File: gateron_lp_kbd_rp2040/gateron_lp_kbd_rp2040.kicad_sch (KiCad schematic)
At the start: 238 parts, among them J1 TYPE-C-31-M-12, J2 JST-SH-2 SM02B, Q1 DMG3415U, SW1 KS-33, SW10 KS-33, SW11 KS-33, SW12 KS-33, SW13 KS-33, SW14 KS-33, SW15 KS-33, SW16 KS-33, SW17 KS-33, SW18 KS-33, SW19 KS-33, SW2 KS-33, SW20 KS-33, SW21 KS-33, SW22 KS-33, SW23 KS-33, SW24 KS-33, SW25 KS-33, SW26 KS-33, SW27 KS-33, SW28 KS-33, SW29 KS-33, SW3 KS-33, SW30 KS-33, SW31 KS-33, SW32 KS-33, SW33 KS-33, SW34 KS-33, SW35 KS-33, SW36 KS-33, SW37 KS-33, SW38 KS-33, SW39 KS-33, SW4 KS-33, SW40 KS-33, SW41 KS-33, SW42 KS-33, SW43 KS-33, SW44 KS-33, SW45 KS-33, SW46 KS-33, SW47 KS-33, SW48 KS-33, SW49 KS-33, SW5 KS-33, SW50 KS-33, SW51 KS-33, SW52 KS-33, SW53 KS-33, SW54 2U, SW55 KS-33, SW56 KS-33, SW57 KS-33, SW58 KS-33, SW59 KS-33, SW6 KS-33, SW60 RESET, SW61 BOOTSEL (VERIFY), SW62 PWR MSK-12C02, SW7 KS-33, SW8 KS-33, SW9 KS-33, U1 RP2040, U2 MCP73831-2ACI/OT, U3 AP2112K-3.3, U4 USBLC6-2SC6, U5 W25Q16JVUXIQ, U6 CYW43439, U7 74AHCT1G125, Y1 12MHz, Y2 37.4MHz

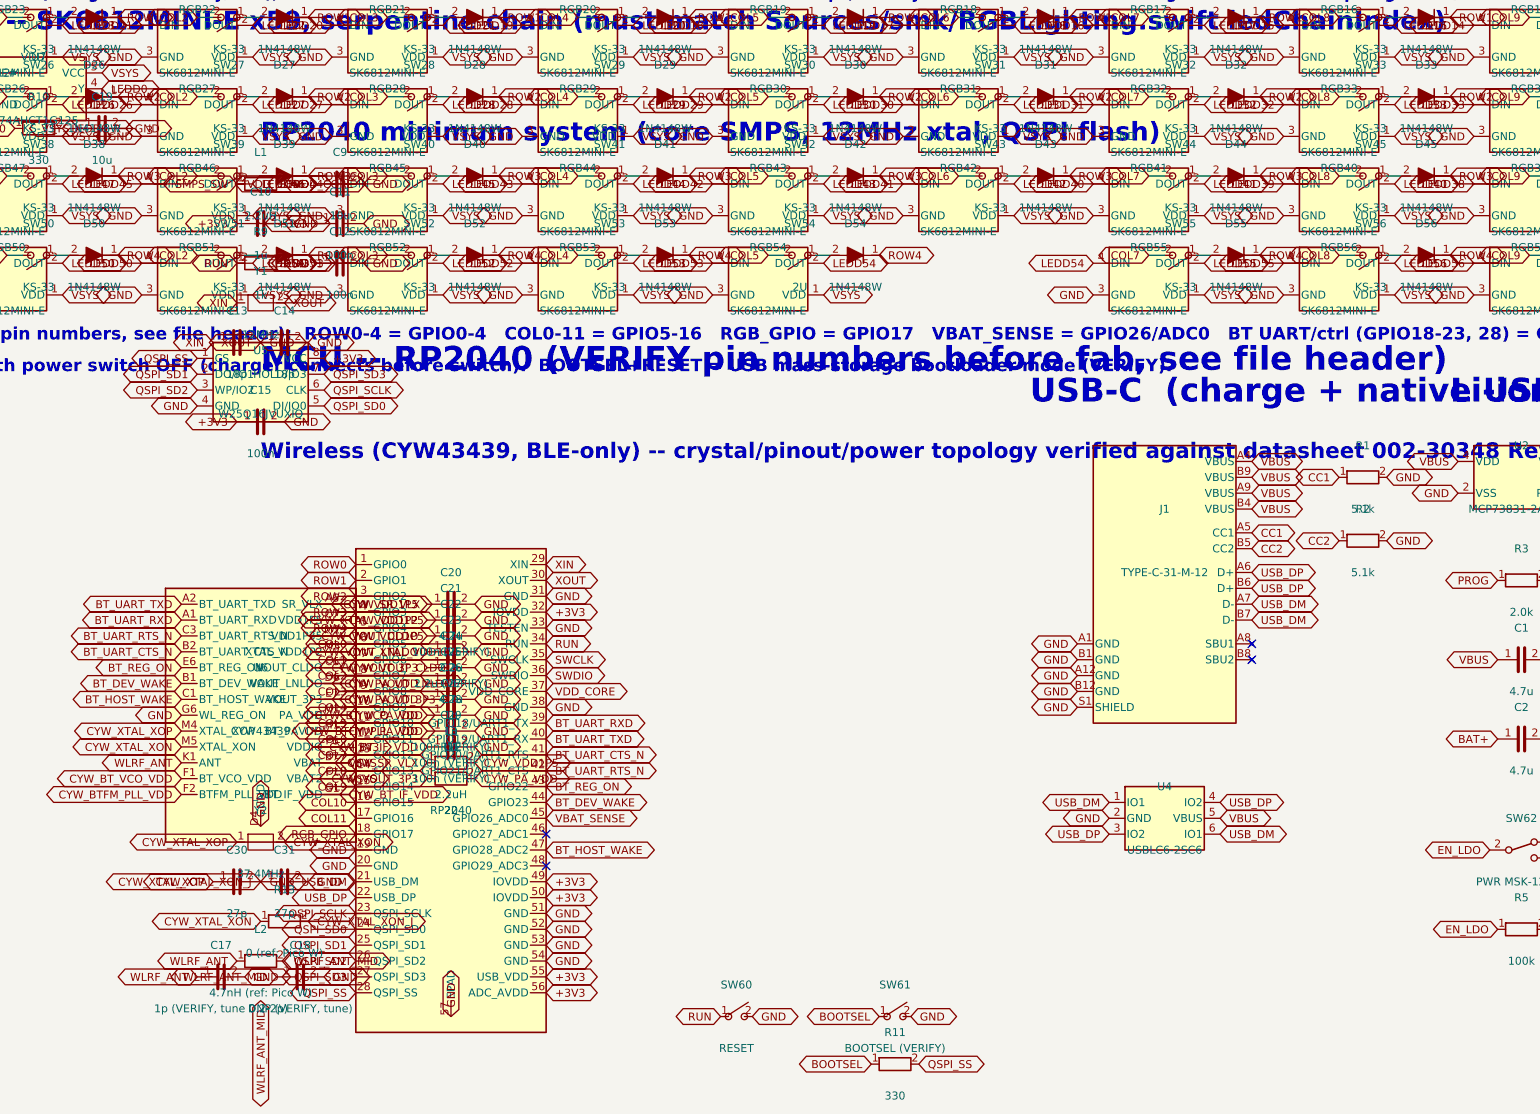
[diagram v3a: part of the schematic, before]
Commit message: Verify RP2040 pin numbers against the real datasheet, fix two real bugs
Pin numbers, dedicated-pin names, and QFN-56 side rotation now come from
Raspberry Pi's own RP2040 datasheet (Fig. 3, Table 1, Table 2) instead of
an invented sequential scheme. This caught two real design bugs:

- The core supply was modeled as a buck regulator needing an external
  inductor (L1, 2.2uH). The real on-chip regulator (Section 2.10, "Core
  Supply Regulator") is a linear/LDO type -- VREG_VIN -> VREG_VOUT -> DVDD
  -- needing only decoupling capacitors. L1 is removed; C9/C32/C33/C34 now
  match the datasheet's own application circuit (Figure 20).
- The BT UART was wired to GPIO18-21, but UART1's real alternate-function
  pins are GPIO20-23 (Table 2) -- GPIO18/19 (no alt-function needed) now
  carry BT_REG_ON/BT_DEV_WAKE instead, freeing GPIO20-23 for the actual
  UART1 TX/RX/CTS/RTS.

Also fixed: the real chip has no perimeter GND pins (GND is only the
single exposed thermal pad) -- removed several invented ones. And caught,
independently of the pinout work, two schematic label collisions (C13/C14
and C30/C31 crystal load caps landing global labels of different nets on
the identical coordinate, which can short a net to GND in the extracted
netlist) -- widened spacing to fix both.

Verified via kicad-happy analyzers: zero new errors/warnings, zero
courtyard or keepout collisions, zero schematic label collisions anywhere
in the file (full-file scan, not just the touched areas).

Co-Authored-By: Claude Sonnet 5 <noreply@anthropic.com>
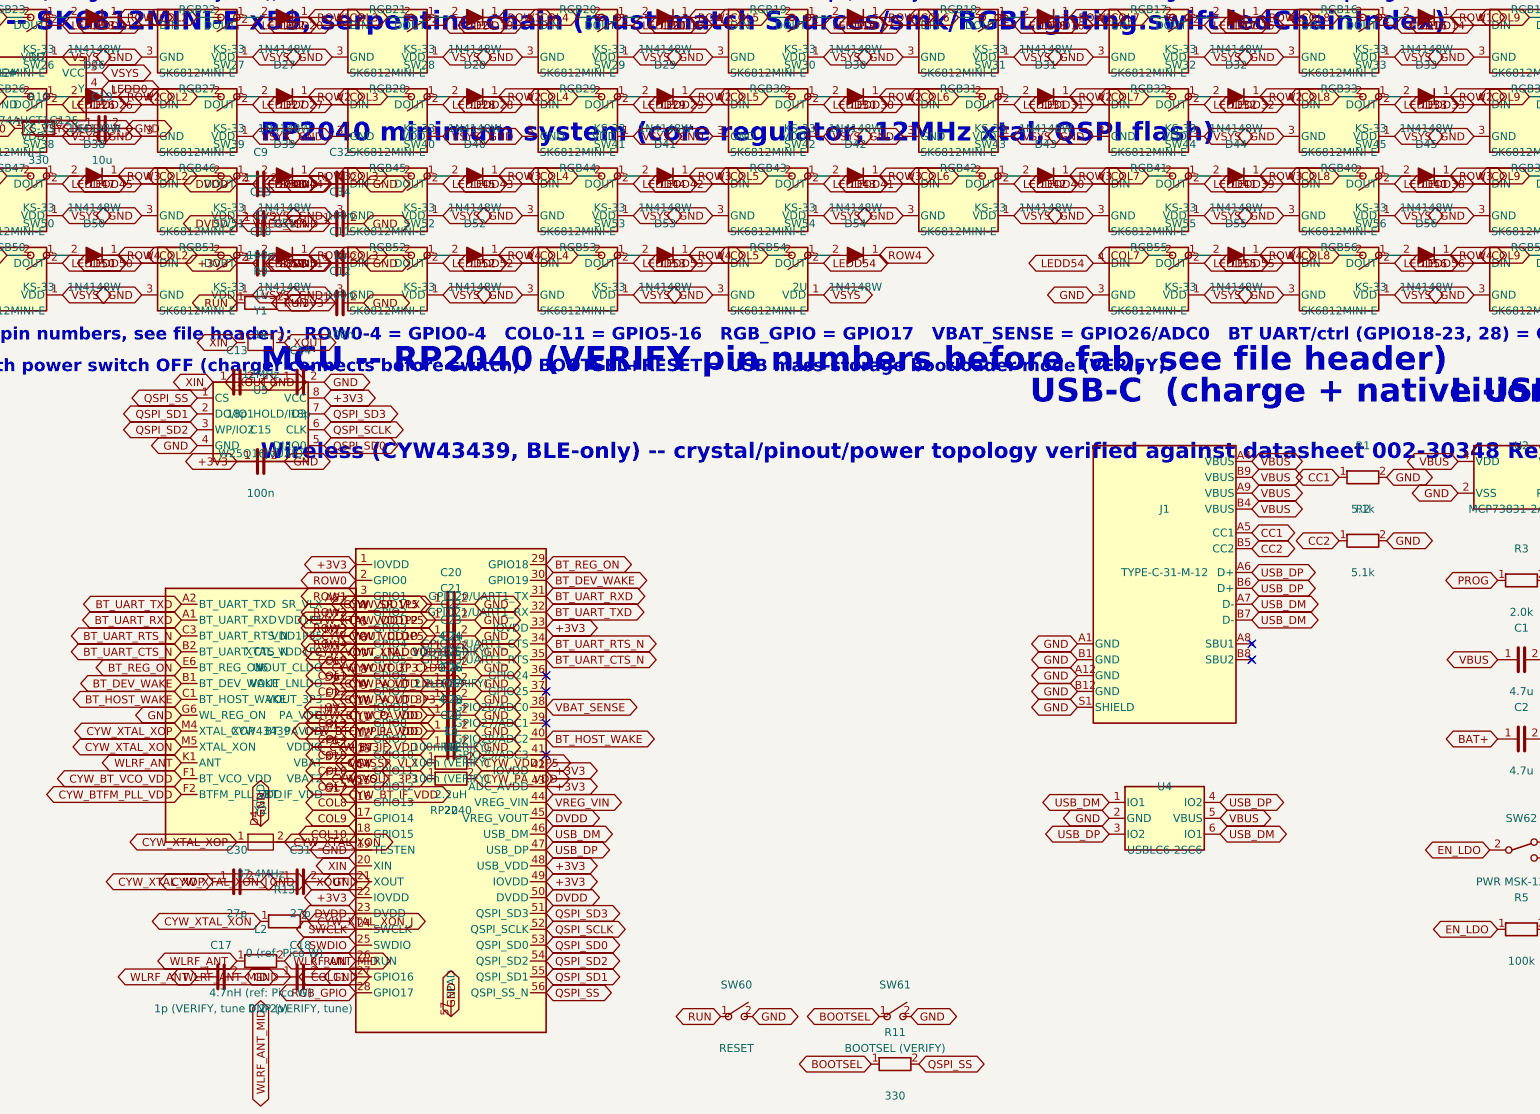
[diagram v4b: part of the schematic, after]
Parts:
- removed L1: 2.2uH, kbd:RC_0603, symbol kbd:R_kbd
- added C32, C33: 100n, kbd:RC_0603, symbol kbd:C_kbd
- added C34: 1u, kbd:RC_0603, symbol kbd:C_kbd
- C9: value 10u -> 1u
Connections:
- net +3V3: now also U1.1 (IOVDD), U1.10 (IOVDD), U1.22 (IOVDD), U1.33 (IOVDD), U1.42 (IOVDD), U1.43 (ADC_AVDD), U1.48 (USB_VDD); no longer U1.32 (IOVDD), U1.50 (IOVDD), U1.55 (USB_VDD), U1.56 (ADC_AVDD)
- net BT_DEV_WAKE: now also U1.30 (GPIO19); no longer U1.44 (GPIO23)
- net BT_HOST_WAKE: now also U1.40 (GPIO28/ADC2); no longer U1.47 (GPIO28_ADC2)
- net BT_REG_ON: now also U1.29 (GPIO18); no longer U1.43 (GPIO22)
- net BT_UART_CTS_N: now also U1.35 (GPIO23/UART1_RTS); no longer U1.41 (GPIO20/UART1_RTS)
- net BT_UART_RTS_N: now also U1.34 (GPIO22/UART1_CTS); no longer U1.42 (GPIO21/UART1_CTS)
- net BT_UART_RXD: now also U1.31 (GPIO20/UART1_TX); no longer U1.39 (GPIO18/UART1_TX)
- net BT_UART_TXD: now also U1.32 (GPIO21/UART1_RX); no longer U1.40 (GPIO19/UART1_RX)
- net COL0: now also U1.7 (GPIO5); no longer U1.6 (GPIO5)
- net COL1: now also U1.8 (GPIO6); no longer U1.7 (GPIO6)
- net COL10: now also U1.18 (GPIO15); no longer U1.16 (GPIO15)
- net COL11: now also U1.27 (GPIO16); no longer U1.17 (GPIO16)
- net COL2: now also U1.9 (GPIO7); no longer U1.8 (GPIO7)
- net COL3: now also U1.11 (GPIO8); no longer U1.9 (GPIO8)
- net COL4: now also U1.12 (GPIO9); no longer U1.10 (GPIO9)
- net COL5: now also U1.13 (GPIO10); no longer U1.11 (GPIO10)
- net COL6: now also U1.14 (GPIO11); no longer U1.12 (GPIO11)
- net COL7: now also U1.15 (GPIO12); no longer U1.13 (GPIO12)
- net COL8: now also U1.16 (GPIO13); no longer U1.14 (GPIO13)
- net COL9: now also U1.17 (GPIO14); no longer U1.15 (GPIO14)
- net CYW_XTAL_XON_J: no longer C1.2, C10.2, C11.2, C12.2, C13.2, C14.1, C14.2, C15.2, C17.2, C18.2, C19.2, C2.2, C20.2, C21.2, C22.2, C23.2, C24.2, C25.2, C26.2, C27.2, C28.2, C29.2, C3.2, C30.2, C31.2, C4.2, C5.2, C7.2, C8.2, C9.2, J1.A1 (GND), J1.A12 (GND), J1.B1 (GND), J1.B12 (GND), J1.S1 (SHIELD), J2.2 (BAT-), R1.2, R2.2, R3.2, R5.2, R7.2, RGB1.3 (GND), RGB10.3 (GND), RGB11.3 (GND), RGB12.3 (GND), RGB13.3 (GND), RGB14.3 (GND), RGB15.3 (GND), RGB16.3 (GND), RGB17.3 (GND), RGB18.3 (GND), RGB19.3 (GND), RGB2.3 (GND), RGB20.3 (GND), RGB21.3 (GND), RGB22.3 (GND), RGB23.3 (GND), RGB24.3 (GND), RGB25.3 (GND), RGB26.3 (GND), RGB27.3 (GND), RGB28.3 (GND), RGB29.3 (GND), RGB3.3 (GND), RGB30.3 (GND), RGB31.3 (GND), RGB32.3 (GND), RGB33.3 (GND), RGB34.3 (GND), RGB35.3 (GND), RGB36.3 (GND), RGB37.3 (GND), RGB38.3 (GND), RGB39.3 (GND), RGB4.3 (GND), RGB40.3 (GND), RGB41.3 (GND), RGB42.3 (GND), RGB43.3 (GND), RGB44.3 (GND), RGB45.3 (GND), RGB46.3 (GND), RGB47.3 (GND), RGB48.3 (GND), RGB49.3 (GND), RGB5.3 (GND), RGB50.3 (GND), RGB51.3 (GND), RGB52.3 (GND), RGB53.3 (GND), RGB54.3 (GND), RGB55.3 (GND), RGB56.3 (GND), RGB57.3 (GND), RGB58.3 (GND), RGB59.3 (GND), RGB6.3 (GND), RGB7.3 (GND), RGB8.3 (GND), RGB9.3 (GND), SW60.2, SW61.2, SW62.3 (B), U1.19 (GND), U1.20 (GND), U1.30 (XOUT), U1.31 (GND), U1.33 (TESTEN), U1.38 (GND), U1.51 (GND), U1.52 (GND), U1.53 (GND), U1.54 (GND), U1.57 (EPAD), U2.2 (VSS), U3.2 (GND), U4.2 (GND), U5.4 (GND), U6.D4 (GND), U6.G6 (WL_REG_ON), U7.1 (OE#), U7.3 (GND), Y1.2
- net QSPI_SCLK: now also U1.52 (QSPI_SCLK); no longer U1.23 (QSPI_SCLK)
- net QSPI_SD0: now also U1.53 (QSPI_SD0); no longer U1.24 (QSPI_SD0)
- net QSPI_SD1: now also U1.55 (QSPI_SD1); no longer U1.25 (QSPI_SD1)
- net QSPI_SD2: now also U1.54 (QSPI_SD2); no longer U1.26 (QSPI_SD2)
- net QSPI_SD3: now also U1.51 (QSPI_SD3); no longer U1.27 (QSPI_SD3)
- net QSPI_SS: now also U1.56 (QSPI_SS_N); no longer U1.28 (QSPI_SS)
- net RGB_GPIO: now also U1.28 (GPIO17); no longer U1.18 (GPIO17)
- net ROW0: now also U1.2 (GPIO0); no longer U1.1 (GPIO0)
- net ROW1: now also U1.3 (GPIO1); no longer U1.2 (GPIO1)
- net ROW2: now also U1.4 (GPIO2); no longer U1.3 (GPIO2)
- net ROW3: now also U1.5 (GPIO3); no longer U1.4 (GPIO3)
- net ROW4: now also U1.6 (GPIO4); no longer U1.5 (GPIO4)
- net RUN: now also U1.26 (RUN); no longer U1.34 (RUN)
- net SWCLK: now also U1.24 (SWCLK); no longer U1.35 (SWCLK)
- net SWDIO: now also U1.25 (SWDIO); no longer U1.36 (SWDIO)
- net USB_DM: now also U1.46 (USB_DM); no longer U1.21 (USB_DM)
- net USB_DP: now also U1.47 (USB_DP); no longer U1.22 (USB_DP)
- net VBAT_SENSE: now also U1.38 (GPIO26/ADC0); no longer U1.45 (GPIO26_ADC0)
- net XIN: now also U1.20 (XIN); no longer U1.29 (XIN)
- net VDD_CORE: no longer names the net of U1.37 (GPIO25)
- net VDD_CORE: no longer C9.1
- new net DVDD: C32.1, C33.1, C9.1, U1.23 (DVDD), U1.45 (VREG_VOUT), U1.50 (DVDD)
- new net GND: C1.2, C10.2, C11.2, C12.2, C13.2, C14.2, C15.2, C17.2, C18.2, C19.2, C2.2, C20.2, C21.2, C22.2, C23.2, C24.2, C25.2, C26.2, C27.2, C28.2, C29.2, C3.2, C30.2, C31.2, C32.2, C33.2, C34.2, C4.2, C5.2, C7.2, C8.2, C9.2, J1.A1 (GND), J1.A12 (GND), J1.B1 (GND), J1.B12 (GND), J1.S1 (SHIELD), J2.2 (BAT-), R1.2, R2.2, R3.2, R5.2, R7.2, RGB1.3 (GND), RGB10.3 (GND), RGB11.3 (GND), RGB12.3 (GND), RGB13.3 (GND), RGB14.3 (GND), RGB15.3 (GND), RGB16.3 (GND), RGB17.3 (GND), RGB18.3 (GND), RGB19.3 (GND), RGB2.3 (GND), RGB20.3 (GND), RGB21.3 (GND), RGB22.3 (GND), RGB23.3 (GND), RGB24.3 (GND), RGB25.3 (GND), RGB26.3 (GND), RGB27.3 (GND), RGB28.3 (GND), RGB29.3 (GND), RGB3.3 (GND), RGB30.3 (GND), RGB31.3 (GND), RGB32.3 (GND), RGB33.3 (GND), RGB34.3 (GND), RGB35.3 (GND), RGB36.3 (GND), RGB37.3 (GND), RGB38.3 (GND), RGB39.3 (GND), RGB4.3 (GND), RGB40.3 (GND), RGB41.3 (GND), RGB42.3 (GND), RGB43.3 (GND), RGB44.3 (GND), RGB45.3 (GND), RGB46.3 (GND), RGB47.3 (GND), RGB48.3 (GND), RGB49.3 (GND), RGB5.3 (GND), RGB50.3 (GND), RGB51.3 (GND), RGB52.3 (GND), RGB53.3 (GND), RGB54.3 (GND), RGB55.3 (GND), RGB56.3 (GND), RGB57.3 (GND), RGB58.3 (GND), RGB59.3 (GND), RGB6.3 (GND), RGB7.3 (GND), RGB8.3 (GND), RGB9.3 (GND), SW60.2, SW61.2, SW62.3 (B), U1.19 (TESTEN), U1.57 (EPAD), U2.2 (VSS), U3.2 (GND), U4.2 (GND), U5.4 (GND), U6.D4 (GND), U6.G6 (WL_REG_ON), U7.1 (OE#), U7.3 (GND)
- new net VREG_VIN: C34.1, U1.44 (VREG_VIN)
- new net XOUT: C14.1, U1.21 (XOUT), Y1.2
- no-connect marks 6 -> 8
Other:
- note added: "RP2040 minimum system (core regulator, 12MHz xtal, QSPI flash)"
- note removed: "RP2040 minimum system (core SMPS, 12MHz xtal, QSPI flash)"
- moved on the sheet: C10, C11, C12, C13, C14, C15, C31, C9, R9, U5, Y1

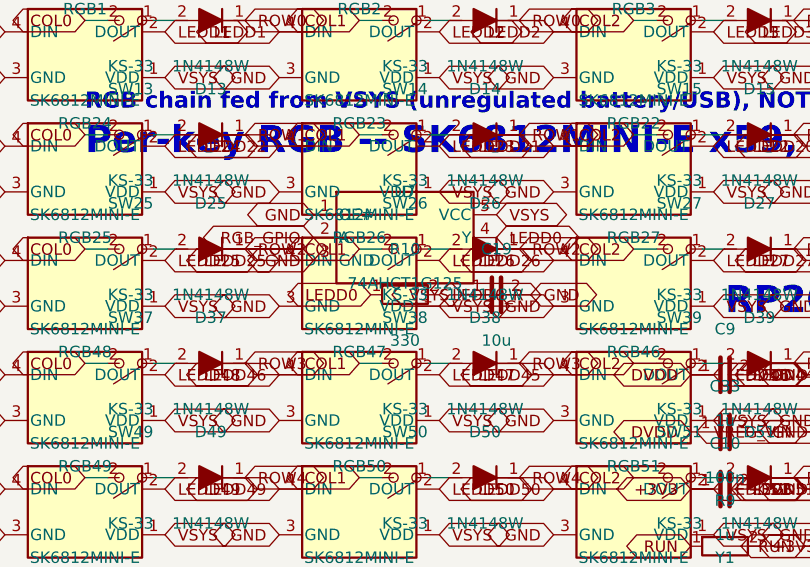
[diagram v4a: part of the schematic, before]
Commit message: Verify RGB level shifter part number against real datasheets
Confirmed the level shifter (U7) against TI's SN74AHCT1G125-Q1 datasheet
(SCLS504E): pinout (OE/A/GND/Y/VCC) already matched exactly, and TI's
"DBV" package is indeed SOT-23-5, matching this file's footprint.

Pinned the value to the specific TI part (SN74AHCT1G125DBVR) instead of
the bare "74AHCT1G125" family name, since it turns out not every same-
numbered part is a drop-in here: Nexperia's own 74AHCT1G125 doesn't come
in SOT-23-5 at all (only TSSOP5/SC-74A/XSON6/XSON5), and specs a narrower
4.5-5.5V VCC range. TI's part specs 3-5.5V, which matters because this
chip's VCC is fed from VSYS (the unregulated battery/USB rail), which can
drop to ~3.0V on battery -- below Nexperia's guaranteed range.

Co-Authored-By: Claude Sonnet 5 <noreply@anthropic.com>
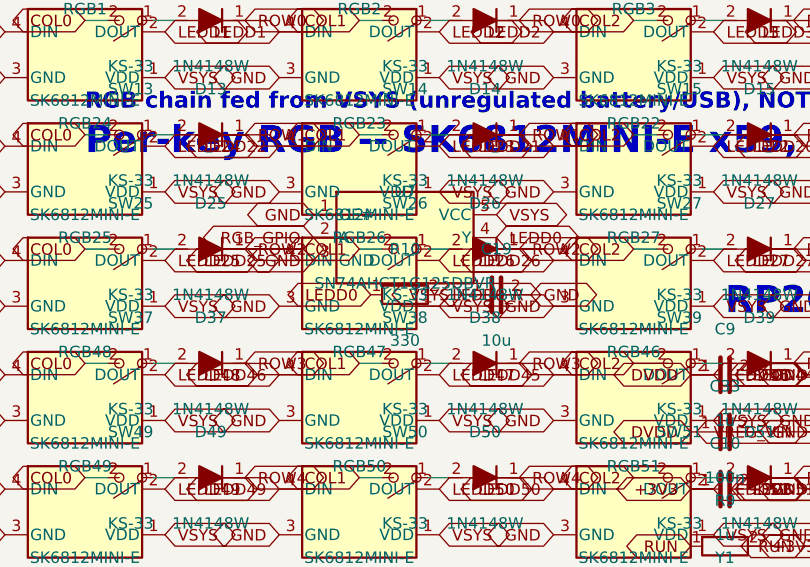
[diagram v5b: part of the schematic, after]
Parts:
- U7: value 74AHCT1G125 -> SN74AHCT1G125DBVR
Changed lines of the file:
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@@
     (exclude_from_sim no) (in_bom yes) (on_board yes) (dnp no) (fields_autoplaced yes)
     (property "Reference" "U7" (at 60.96 49.53 0) (effects (font (size 1.27 1.27))))
-    (property "Value" "74AHCT1G125" (at 60.96 59.69 0) (effects (font (size 1.27 1.27))))
+    (property "Value" "SN74AHCT1G125DBVR" (at 60.96 59.69 0) (effects (font (size 1.27 1.27))))
     (property "Footprint" "kbd:SOT-23-5" (at 60.96 54.61 0) (effects (font (size 1.27 1.27)) (hide yes)))
     (property "Datasheet" "~" (at 60.96 54.61 0) (effects (font (size 1.27 1.27)) (hide yes)))

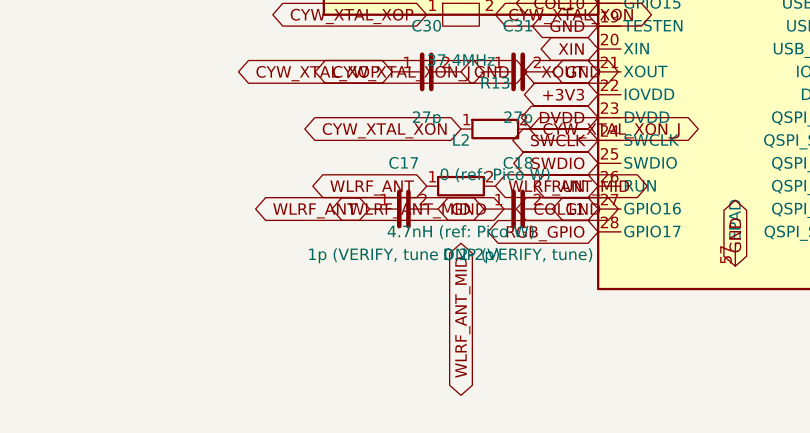
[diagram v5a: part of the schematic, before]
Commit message: Add a real antenna and fix keepout semantics -- fills a real design gap
Verification turned up more than unverified values here: the antenna
keepout zone existed but had NO actual antenna connected to it (WLRF_ANT_MID
dead-ended at the DNP C18 with nothing beyond it), and the zone's own rules
(pads/footprints not_allowed) would have made it impossible to ever place
a real antenna there -- backwards from how antenna keepouts actually work
(they keep the ground plane/pour and stitching vias away; they don't
forbid the antenna's own footprint or feed trace).

Fixed both:
- Added a real, purchasable 2.4GHz chip antenna (Johanson 2450AT18B100E,
  datasheet Ver. 4.0 2018: 2400-2500MHz, 50 ohm, 1=FEED/2=NC, body
  3.2x1.6x1.3mm) inside the keepout zone.
- Corrected the keepout to (tracks allowed) (vias not_allowed)
  (pads allowed) (copperpour not_allowed) (footprints allowed) -- so it
  actually protects the antenna from ground-plane detuning instead of
  forbidding the antenna from existing.
- Switched L2/C17's matching values from the Pico W's own reference
  (tuned for Abracon/Proant's completely different, proprietary PCB-trace
  antenna) to Johanson's own published matching-network reference for
  this specific chip antenna (2.7nH series inductor, 1.2pF shunt cap,
  against a 50-ohm source) -- a better-grounded starting point now that
  the antenna itself has changed.

Verified via kicad-happy analyzers: zero courtyard collisions, zero
schematic label collisions, only an expected false-positive keepout
finding (the analyzer's heuristic doesn't parse the zone's per-property
allow/not_allow settings; the generated zone text confirms they're
correct). Still open: the feed trace itself isn't drawn (unrouted by
design), and the matching values still need real RF tuning on this
board's own layout.

Co-Authored-By: Claude Sonnet 5 <noreply@anthropic.com>
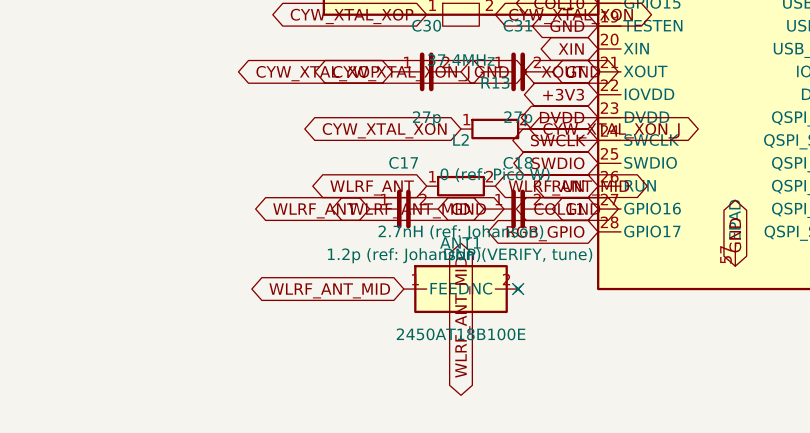
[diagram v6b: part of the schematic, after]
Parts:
- added ANT1: 2450AT18B100E, kbd:ANT_JOHANSON_2450AT18B100, symbol kbd:ANT_JOHANSON
- C17: value 1p (VERIFY, tune 0.2-2p) -> 1.2p (ref: Johanson)
- L2: value 4.7nH (ref: Pico W) -> 2.7nH (ref: Johanson)
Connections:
- net WLRF_ANT_MID: now also ANT1.1 (FEED)
- no-connect marks 8 -> 9
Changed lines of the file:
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@@
     (exclude_from_sim no) (in_bom yes) (on_board yes) (dnp no) (fields_autoplaced yes)
     (property "Reference" "L2" (at 96.52 189.23 0) (effects (font (size 1.27 1.27))))
-    (property "Value" "4.7nH (ref: Pico W)" (at 96.52 199.39 0) (effects (font (size 1.27 1.27))))
+    (property "Value" "2.7nH (ref: Johanson)" (at 96.52 199.39 0) (effects (font (size 1.27 1.27))))
     (property "Footprint" "kbd:RC_0201" (at 96.52 194.31 0) (effects (font (size 1.27 1.27)) (hide yes)))
     (property "Datasheet" "~" (at 96.52 194.31 0) (effects (font (size 1.27 1.27)) (hide yes)))
@@
     (exclude_from_sim no) (in_bom yes) (on_board yes) (dnp no) (fields_autoplaced yes)
     (property "Reference" "C17" (at 90.17 191.77 0) (effects (font (size 1.27 1.27))))
-    (property "Value" "1p (VERIFY, tune 0.2-2p)" (at 90.17 201.93 0) (effects (font (size 1.27 1.27))))
+    (property "Value" "1.2p (ref: Johanson)" (at 90.17 201.93 0) (effects (font (size 1.27 1.27))))
     (property "Footprint" "kbd:RC_0402" (at 90.17 196.85 0) (effects (font (size 1.27 1.27)) (hide yes)))
     (property "Datasheet" "~" (at 90.17 196.85 0) (effects (font (size 1.27 1.27)) (hide yes)))
@@
     (instances (project "gateron_lp_kbd_rp2040" (path "/a2643ac4-cbbd-530c-93c4-588f70f6c903" (reference "C18") (unit 1))))
   )
+  (symbol (lib_id "kbd:ANT_JOHANSON") (at 96.52 205.74) (unit 1)
+    (exclude_from_sim no) (in_bom yes) (on_board yes) (dnp no) (fields_autoplaced yes)
+    (property "Reference" "ANT1" (at 96.52 200.66 0) (effects (font (size 1.27 1.27))))
+    (property "Value" "2450AT18B100E" (at 96.52 210.82 0) (effects (font (size 1.27 1.27))))
+    (property "Footprint" "kbd:ANT_JOHANSON_2450AT18B100" (at 96.52 205.74 0) (effects (font (size 1.27 1.27)) (hide yes)))
+    (property "Datasheet" "~" (at 96.52 205.74 0) (effects (font (size 1.27 1.27)) (hide yes)))
+    (property "Description" "" (at 96.52 205.74 0) (effects (font (size 1.27 1.27)) (hide yes)))
+    (pin "1")
+    (pin "2")
+    (instances (project "gateron_lp_kbd_rp2040" (path "/a2643ac4-cbbd-530c-93c4-588f70f6c903" (reference "ANT1") (unit 1))))
+  )
   (symbol (lib_id "kbd:LVL_SHIFT_BUF") (at 60.96 54.61) (unit 1)
     (exclude_from_sim no) (in_bom yes) (on_board yes) (dnp no) (fields_autoplaced yes)
@@
       (effects (font (size 1.27 1.27)) (hide yes)))
   )
+  (global_label "WLRF_ANT_MID" (shape bidirectional) (at 90.17 205.74 180) (fields_autoplaced yes)
+    (effects (font (size 1.27 1.27)) (justify right))
+    (property "Intersheetrefs" "${INTERSHEET_REFS}" (at 90.17 205.74 0)
+      (effects (font (size 1.27 1.27)) (hide yes)))
+  )
   (global_label "GND" (shape bidirectional) (at 50.8 52.07 180) (fields_autoplaced yes)
     (effects (font (size 1.27 1.27)) (justify right))
@@
   (no_connect (at 142.24 156.21))
   (no_connect (at 142.24 161.29))
+  (no_connect (at 102.87 205.74))
   (no_connect (at 369.57 82.55))
   (no_connect (at 255.27 143.51))
